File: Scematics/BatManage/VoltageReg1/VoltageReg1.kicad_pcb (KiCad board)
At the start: 2 copper layers, 8 parts, among them U1 TPS565208

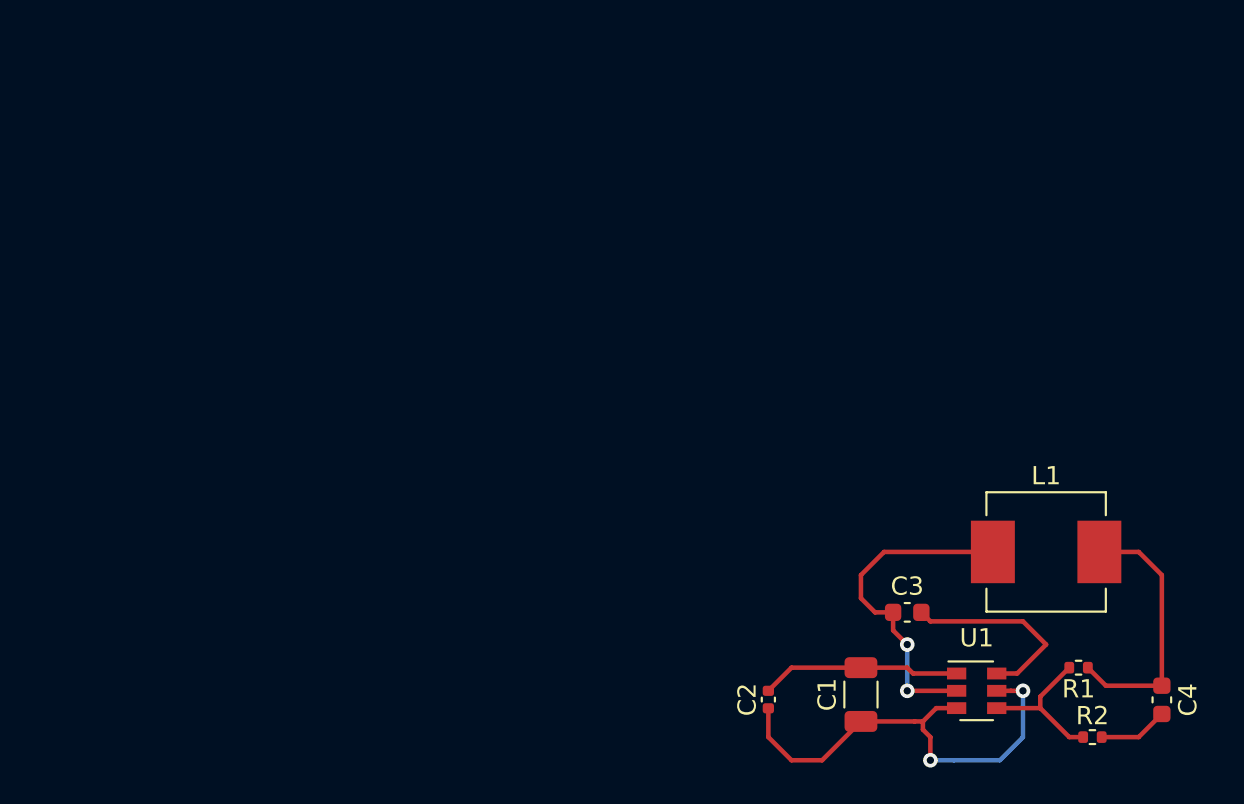
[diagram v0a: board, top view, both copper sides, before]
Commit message: 5V 5A schematic following datahseet layout
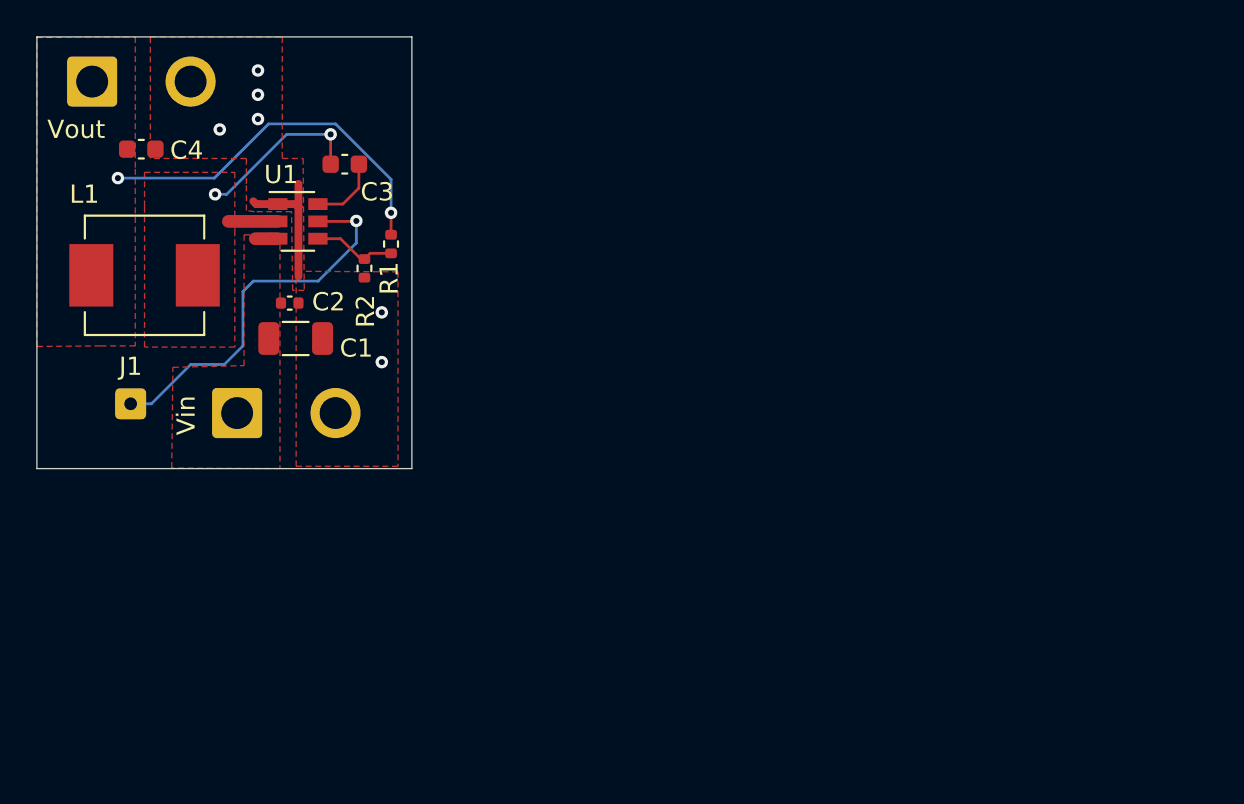
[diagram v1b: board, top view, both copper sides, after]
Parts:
- added J1: Conn_01x01, Connector_Wire:SolderWire-0.127sqmm_1x01_D0.48mm_OD1mm, F.Cu at (47.6, 65.5)
- added Vin: 14.8V, Connector_Wire:SolderWire-1sqmm_1x02_P5.4mm_D1.4mm_OD2.7mm, F.Cu at (53.4, 66.0)
- added Vout: 3, Connector_Wire:SolderWire-1sqmm_1x02_P5.4mm_D1.4mm_OD2.7mm, F.Cu at (45.5, 47.9)
- moved C4 63.6 mm to (48.1, 51.6), turned to 0 degrees
- moved L1 51.7 mm to (48.3, 58.5), turned to 180 degrees
- moved R2 47.5 mm to (60.4, 58.1), turned to 270 degrees
- moved U1 45.3 mm to (56.7, 55.5)
- moved R1 44.3 mm to (61.8, 56.8), turned to 270 degrees
- moved C3 39.5 mm to (59.3, 52.4)
- moved C1 36.7 mm to (56.6, 62.0), turned to 0 degrees
- moved C2 34.1 mm to (56.3, 60.0), turned to 0 degrees
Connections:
- U1 pad 5: Net-(C1-Pad1) -> Net-(J1-Pad1)
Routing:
- net Net-(C1-Pad1): track 25.5 -> 1.24 mm, vias 2 -> 0
- net Net-(J1-Pad1): track 0.00 -> 21.1 mm, vias 0 -> 1
- net Net-(C1-Pad2): track 14.8 -> 7.69 mm, vias 0 -> 6
- net Net-(C3-Pad2): track 10.9 -> 3.92 mm
- net Net-(C3-Pad1): track 18.5 -> 12.1 mm
- net Net-(C4-Pad1): track 14.5 -> 20.5 mm, vias 0 -> 2
- net Net-(R1-Pad2): track 8.28 -> 4.61 mm
- added copper zone on F.Cu, net Net-(C1-Pad1)
- added copper zone on F.Cu, net Net-(C1-Pad2)
- added copper zone on F.Cu, net Net-(C3-Pad1)
- added copper zone on F.Cu, net Net-(C4-Pad1)
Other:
- board outline added: 20.6 x 23.7 mm
- net class Default: clearance 0.2 -> 0.1524; trace_width 0.25 -> 0.1524; via_dia 0.8 -> 0.6858; via_drill 0.4 -> 0.3302
- rule pad_to_mask_clearance: 0 -> 0.0508
- rule trace_clearance: 0.2 -> 0.1524
- rule trace_min: 0.2 -> 0.1524
- rule via_min_drill: 0.3 -> 0.254
- rule via_min_size: 0.4 -> 0.508
